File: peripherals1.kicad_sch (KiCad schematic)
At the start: 0 parts

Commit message: feat: add components to peripherals1
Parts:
- added BZ1: Buzzer, https://www.digikey.com.br/en/products/detail/murata-electronics/PKHPS0013E4000-A2/16399967?s=N4IgTCBcDaIAoGkAScDKAGdBG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, symbol Device:Buzzer
- added C1: 1μ, https://www.digikey.com.br/en/products/detail/samsung-electro-mechanics/CL05A105KO5NNNC/3886725?s=N4IgTCBcDaIMIBkAMBWAg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, symbol Device:C
- added D1, D2, D3, D4, D5: LED_GREEN, symbol Device:LED
- added D2: WS2812B, https://www.digikey.com.br/en/products/detail/feztek/FZ2812-5050/18647407?s=N4IgTCBcDaIGIC0wA4CMYC0BWADLkAugL5A, symbol LED:WS2812B
- added D6: LED_RED, symbol Device:LED
- added D7: LED_YELLOW, symbol Device:LED
- added D8: LED_BLUE, symbol Device:LED
- added MK2: Microphone_Condenser, https://www.digikey.com.br/en/products/detail/same-sky-formerly-cui-devices/CMEJ-0415-42-P/10253451?s=N4IgTCBcDaIMIFkCi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, symbol Device:Microphone_Condenser
- added Q1: Q_NMOS_GSD, https://www.digikey.com.br/en/products/detail/diodes-incorporated/DMN2600UFB-7/4249927?s=N4IgTCBcDaICIFkByYBsAGdBVAYgIQ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, symbol Transistor_FET:Q_NMOS_GSD
- added R1: R_Photo, https://www.digikey.com.br/en/products/detail/harvatek-corporation/B13V1IR-20C000114U1930/13574162?s=N4IgTCBcDaIEIEYDMA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, symbol Device:R_Photo
- added R10, R11, R12, R13, R2, R3, R4, R6, R7, R8, R9: 10k, https://www.digikey.com.br/en/products/detail/yageo/RC0402JR-0710KL/726418?s=N4IgTCBcDaIEoGEAMAWJYBScC0SDsAjEgNIAyIAugL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, symbol Device:R
- added R14, R15, R16, R17, R18, R19, R20, R21: 220, symbol Device:R
- added R22: 1k, https://www.digikey.com.br/en/products/detail/yageo/RC0402JR-071KL/726408, symbol Device:R
- added R5: 2.2k, https://www.digikey.com.br/en/products/detail/panasonic-electronic-components/ERA-2AEB222X/1706013, symbol Device:R
- added RV1, RV2: R_Potentiometer, symbol Device:R_Potentiometer
- added SW1, SW2, SW3, SW4, SW5, SW6, SW7, SW8: SW_Push, https://www.digikey.com.br/en/products/detail/c-k/PTS636SM43SMTR-LFS/10071723?s=N4IgTCBcDaIAoBUDKA2AzCpBZALG7CASgAQAyAY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, symbol Switch:SW_Push
- added U1: TSDP343xx, OptoDevice:Vishay_MOLD-3Pin, symbol Interface_Optical:TSDP343xx
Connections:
- new net: D6.2 (A), R19.2
- new net: R3.1, RV1.3
- new net: D8.2 (A), R21.2
- new net: D1.2 (A), R14.2
- new net: D7.2 (A), R20.2
- new net: MK2.1 (-), R5.2
- new net: D4.2 (A), R17.2
- new net: D5.2 (A), R18.2
- new net: D2.2 (A), R15.2
- new net: D3.2 (A), R16.2
- new net: R4.1, RV2.3
- new net +3V3: C1.1, D2.3 (VDD), Q1.3 (D), R1.1, R10.2, R11.2, R12.2, R13.2, R5.1, R6.2, R7.2, R8.2, R9.2, RV1.1, RV2.1
- new net Button1_GPIO: R6.1, SW1.2
- new net Button2_GPIO: R7.1, SW2.2
- new net Button3_GPIO: R8.1, SW3.2
- new net Button4_GPIO: R9.1, SW4.2
- new net Button5_GPIO: R11.1, SW5.2
- new net Button6_GPIO: R12.1, SW6.2
- new net Button7_GPIO: R13.1, SW7.2
- new net Button8_GPIO: R10.1, SW8.2
- new net Buzzer_GPIO: BZ1.1 (+)
- new net GND: BZ1.2 (-), D1.1 (K), D2.1 (K), D2.1 (VSS), D3.1 (K), D4.1 (K), D5.1 (K), D6.1 (K), D7.1 (K), D8.1 (K), MK2.2 (+), Q1.1 (G), Q1.2 (S), R2.2, R22.2, R3.2, R4.2, SW1.1, SW2.1, SW3.1, SW4.1, SW5.1, SW6.1, SW7.1, SW8.1
- new net LDR_ADC: R1.2, R2.1
- new net LED_blue_GPIO: R21.1
- new net LED_end_GPIO: D2.2 (DIN)
- new net LED_green_GPIO: R14.1, R15.1, R16.1, R17.1, R18.1
- new net LED_red_GPIO: R19.1
- new net LED_yellow_GPIO: R20.1
- new net MOSFET_GPIO: R22.1
- new net Microphone_ADC: C1.2
- new net Potentiometer1_ADC: RV1.2
- new net Potentiometer2_ADC: RV2.2
- no-connect marks 0 -> 1

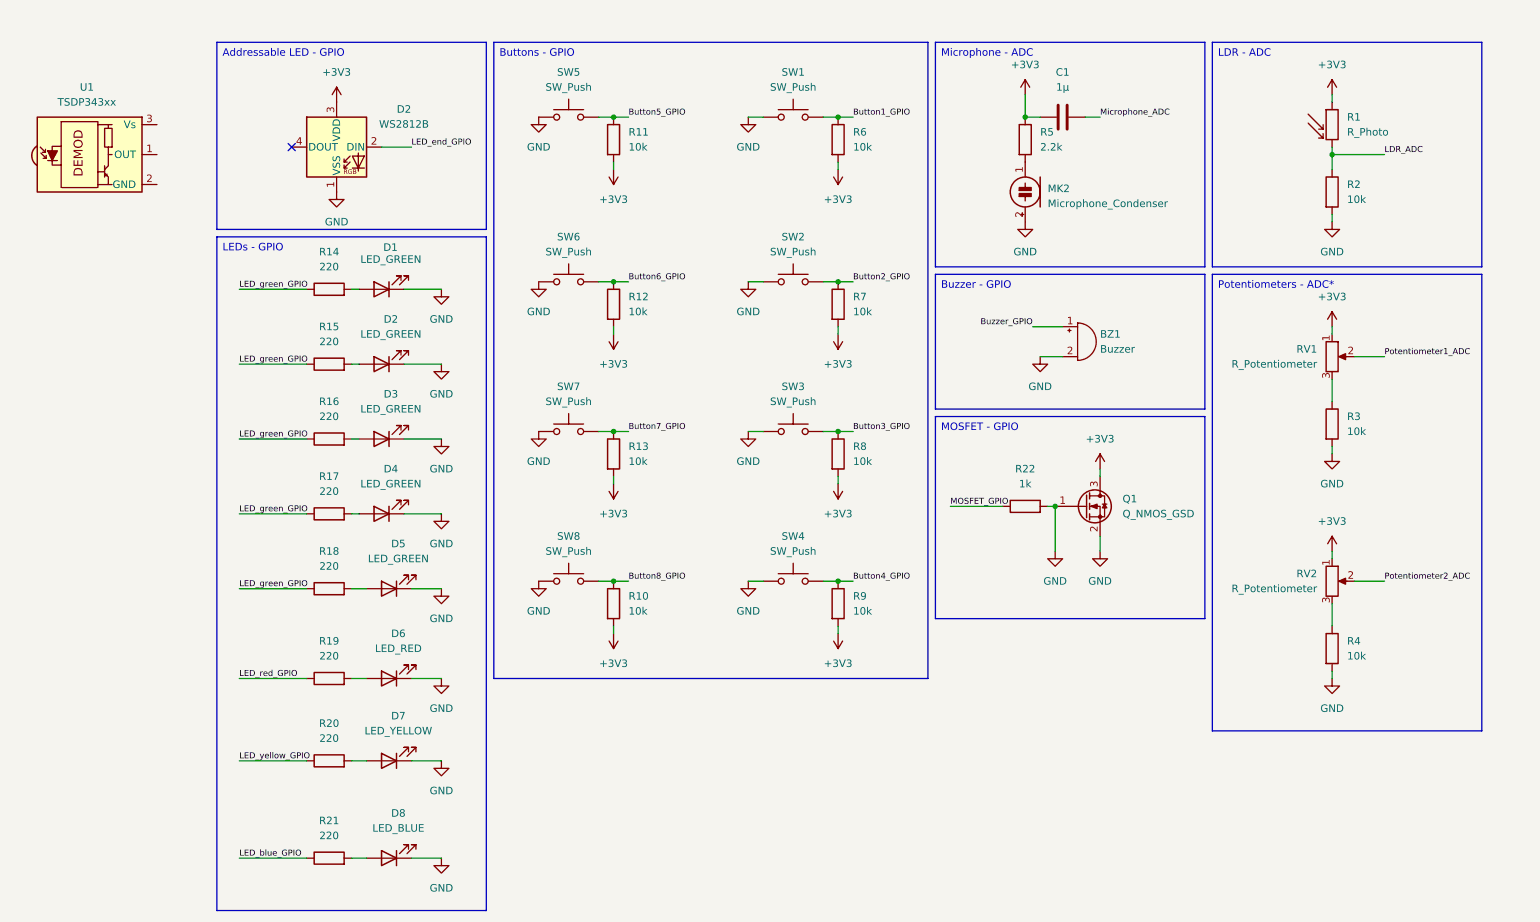
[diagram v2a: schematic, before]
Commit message: refac: changes LED direction, mic output and potentiometer
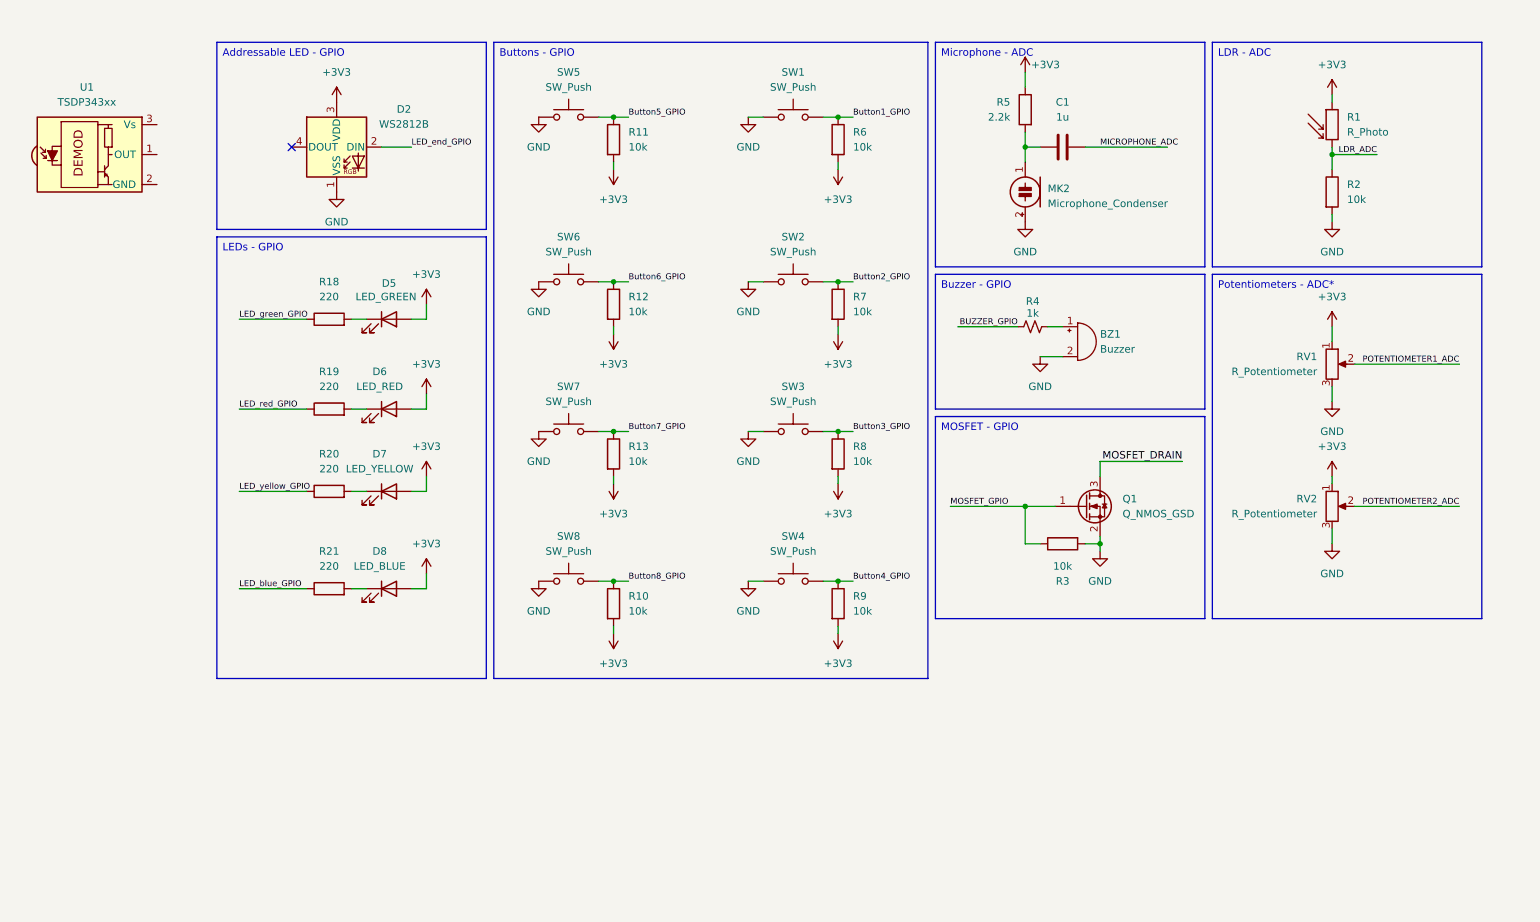
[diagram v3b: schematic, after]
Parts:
- removed D1, D2, D3, D4: LED_GREEN, symbol Device:LED
- removed R14, R15, R16, R17: 220, symbol Device:R
- removed R22: 1k, https://www.digikey.com.br/en/products/detail/yageo/RC0402JR-071KL/726408, symbol Device:R
- removed R4: 10k, https://www.digikey.com.br/en/products/detail/yageo/RC0402JR-0710KL/726418?s=N4IgTCBcDaIEoGEAMAWJYBScC0SDsAjEgNIAyIAugL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, symbol Device:R
- added R4: 1k, Resistor_SMD:R_0402_1005Metric, symbol Device:R_Small_US
- C1: value 1μ -> 1u
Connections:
- net +3V3: now also D5.2 (A), D6.2 (A), D7.2 (A), D8.2 (A); no longer C1.1, Q1.3 (D)
- net GND: now also RV1.3, RV2.3; no longer D5.1 (K), D6.1 (K), D7.1 (K), D8.1 (K), Q1.1 (G)
- net MOSFET_GPIO: now also Q1.1 (G), R3.1
- net at R19.2: now also D6.1 (K); no longer D6.2 (A)
- net at R21.2: now also D8.1 (K); no longer D8.2 (A)
- net at R20.2: now also D7.1 (K); no longer D7.2 (A)
- net at MK2.1 (-), R5.2: now also C1.1
- net at R18.2: now also D5.1 (K); no longer D5.2 (A)
- net Buzzer_GPIO: no longer names the net of BZ1.1 (+)
- net Buzzer_GPIO: now also R4.2
- net Microphone_ADC renamed MICROPHONE_ADC
- net Potentiometer1_ADC renamed POTENTIOMETER1_ADC
- net Potentiometer2_ADC renamed POTENTIOMETER2_ADC
- new net BUZZER_GPIO: R4.1
- new net MOSFET_DRAIN: Q1.3 (D)
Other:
- moved on the sheet: C1, D5, D6, D7, D8, R18, R19, R20, R21, R5, RV1, RV2

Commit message: feat:adds technical informations to components
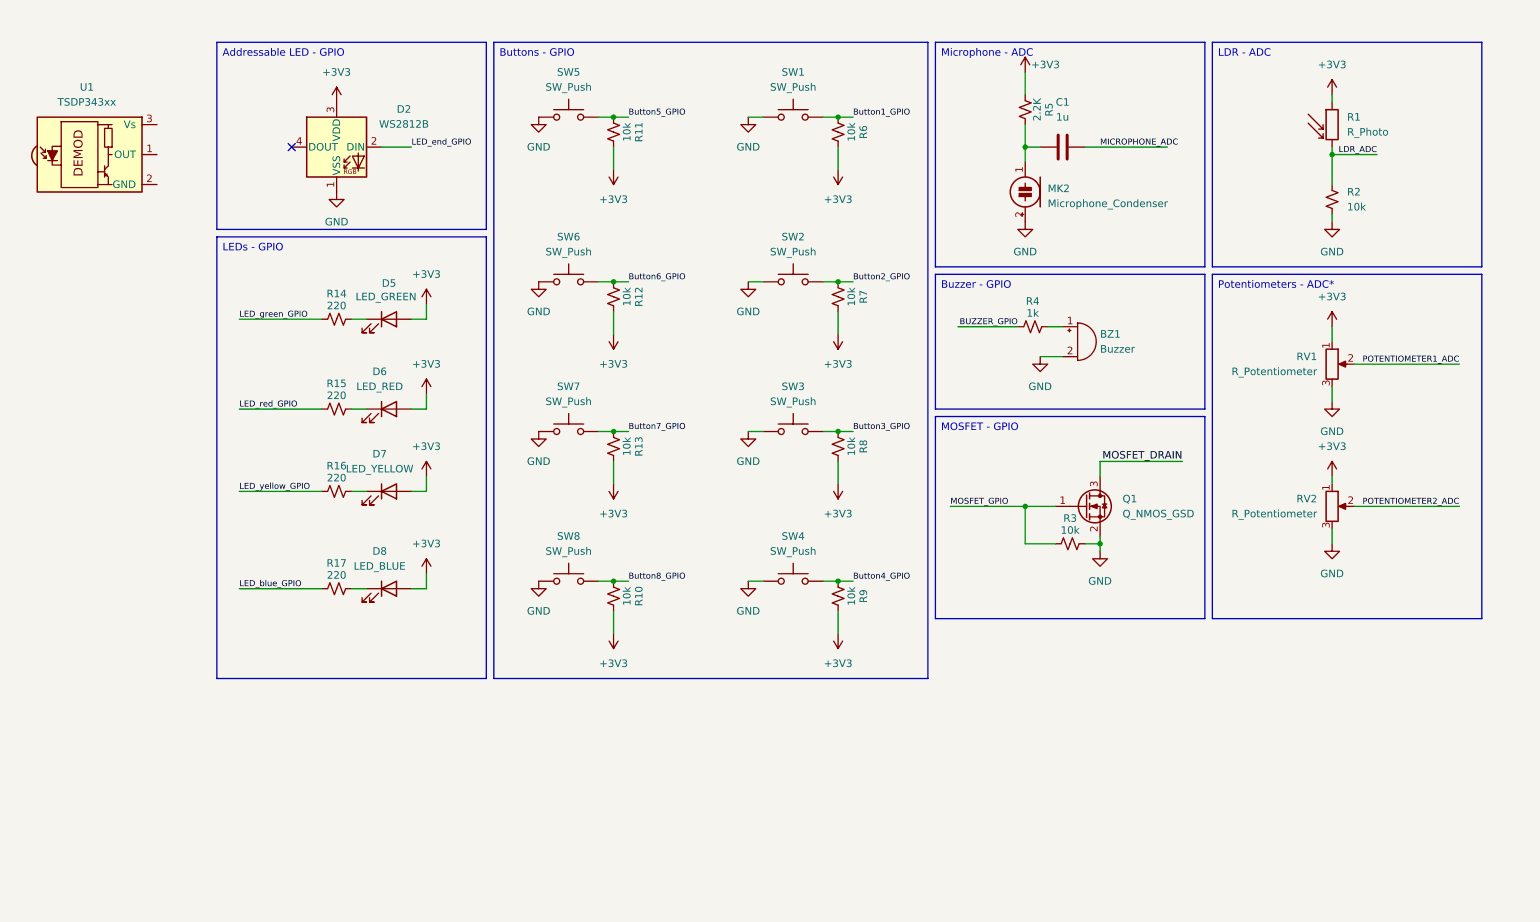
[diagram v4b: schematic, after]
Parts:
- removed R10, R11, R12, R13, R2, R3, R6, R7, R8, R9: 10k, https://www.digikey.com.br/en/products/detail/yageo/RC0402JR-0710KL/726418?s=N4IgTCBcDaIEoGEAMAWJYBScC0SDsAjEgNIAyIAugL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, symbol Device:R
- removed R18, R19, R20, R21: 220, symbol Device:R
- removed R5: 2.2k, https://www.digikey.com.br/en/products/detail/panasonic-electronic-components/ERA-2AEB222X/1706013, symbol Device:R
- added R10, R11, R12, R13, R2, R3, R6, R7, R8, R9: 10k, Resistor_SMD:R_0402_1005Metric, symbol Device:R_Small_US
- added R14, R15, R16, R17: 220, Resistor_SMD:R_0402_1005Metric, symbol Device:R_Small_US
- added R5: 2.2K, Resistor_SMD:R_0402_1005Metric, symbol Device:R_Small_US
- BZ1: footprint https://www.digikey.com.br/en/products/detail/murata-electronics/PKHPS0013E4000-A2/16399967?s=N4IgTCBcDaIAoGkAScDKAGdBG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 -> (none); MPN (none) -> PKHPS0013E4000-A2
- C1: footprint https://www.digikey.com.br/en/products/detail/samsung-electro-mechanics/CL05A105KO5NNNC/3886725?s=N4IgTCBcDaIMIBkAMBWAg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 -> (none); MPN (none) -> CL05A105KO5NNNC
- D2: footprint https://www.digikey.com.br/en/products/detail/feztek/FZ2812-5050/18647407?s=N4IgTCBcDaIGIC0wA4CMYC0BWADLkAugL5A -> (none); MPN (none) -> FZ2812-5050
- D5: MPN (none) -> LGR971-KN-1
- D6: MPN (none) -> QBLP601-R3-2943
- D7: MPN (none) -> LY Q976.01-Q1R2-36-1
- D8: MPN (none) -> LB Q99G.01-P1R1-35-1-5-R18
- MK2: footprint https://www.digikey.com.br/en/products/detail/same-sky-formerly-cui-devices/CMEJ-0415-42-P/10253451?s=N4IgTCBcDaIMIFkCi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 -> (none); MPN (none) -> CMEJ-0415-42-P
- Q1: footprint https://www.digikey.com.br/en/products/detail/diodes-incorporated/DMN2600UFB-7/4249927?s=N4IgTCBcDaICIFkByYBsAGdBVAYgIQ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 -> (none); MPN (none) -> DMN2600UFB-7
- R1: footprint https://www.digikey.com.br/en/products/detail/harvatek-corporation/B13V1IR-20C000114U1930/13574162?s=N4IgTCBcDaIEIEYDMA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 -> (none); MPN (none) -> FZ2812-5050
- SW1, SW2, SW3, SW4, SW5, SW6, SW7, SW8: footprint https://www.digikey.com.br/en/products/detail/c-k/PTS636SM43SMTR-LFS/10071723?s=N4IgTCBcDaIAoBUDKA2AzCpBZALG7CASgAQAyAY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 -> (none); MPN (none) -> PTS636SM43SMTR LFS
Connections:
- net +3V3: now also R10.2, R11.2, R12.2, R13.2, R5.1, R6.2, R7.2, R8.2, R9.2
- net Button1_GPIO: now also R6.1
- net Button2_GPIO: now also R7.1
- net Button3_GPIO: now also R8.1
- net Button4_GPIO: now also R9.1
- net Button5_GPIO: now also R11.1
- net Button6_GPIO: now also R12.1
- net Button7_GPIO: now also R13.1
- net Button8_GPIO: now also R10.1
- net GND: now also R2.2, R3.2
- net LDR_ADC: now also R2.1
- net LED_blue_GPIO: now also R17.1
- net LED_green_GPIO: now also R14.1
- net LED_red_GPIO: now also R15.1
- net LED_yellow_GPIO: now also R16.1
- net MOSFET_GPIO: now also R3.1
- net at D6.1 (K): now also R15.2
- net at D8.1 (K): now also R17.2
- net at D7.1 (K): now also R16.2
- net at C1.1, MK2.1 (-): now also R5.2
- net at D5.1 (K): now also R14.2

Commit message: refac: reannotates designators
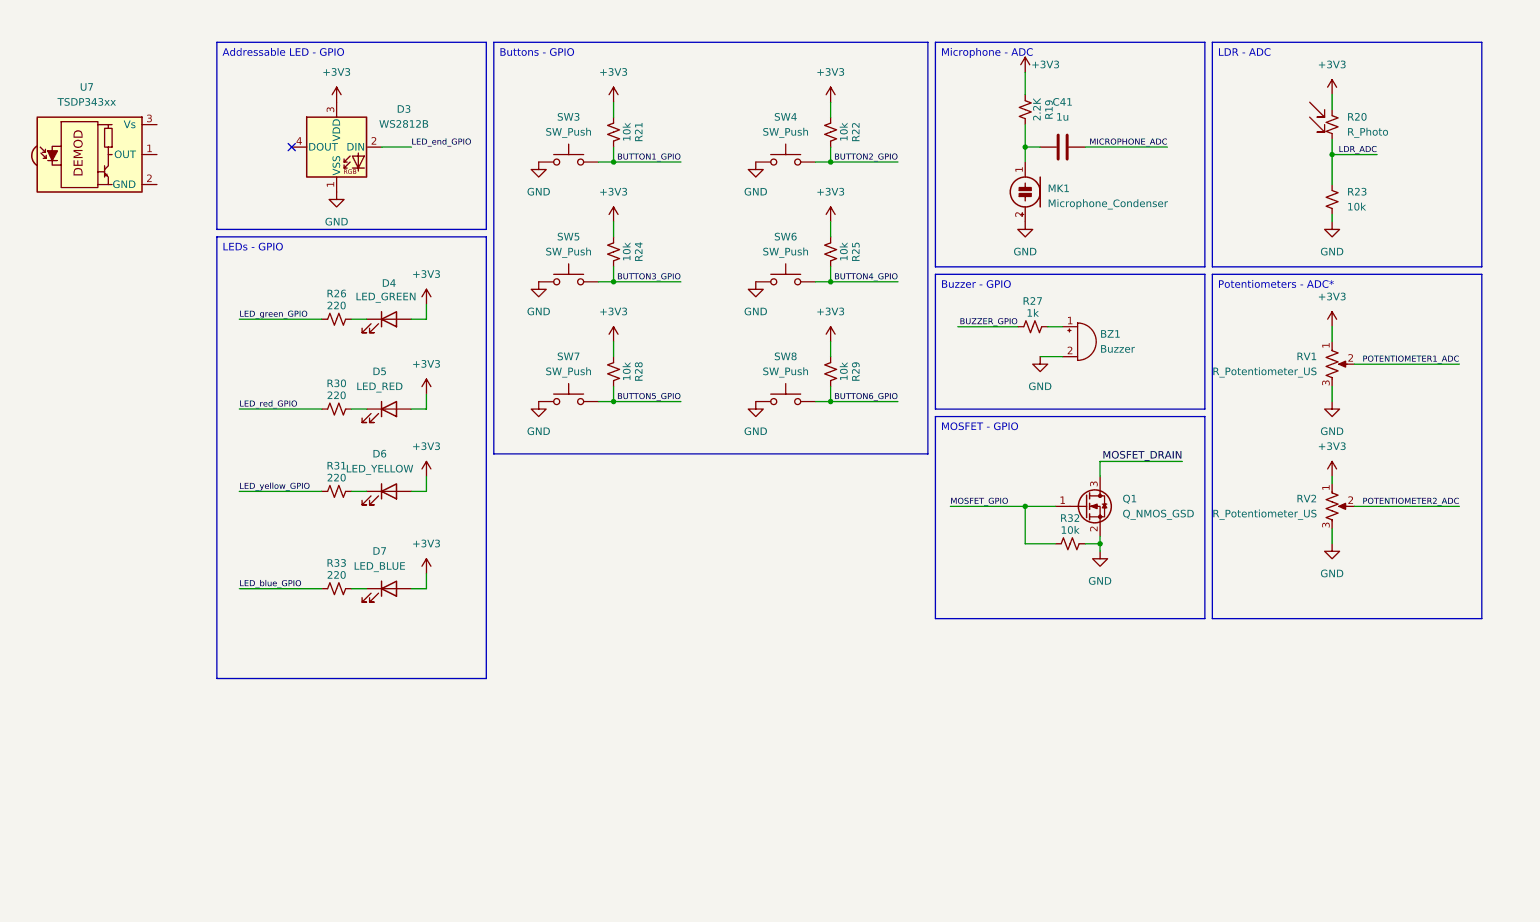
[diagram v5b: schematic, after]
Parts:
- removed R1: R_Photo, symbol Device:R_Photo
- removed R10, R12, R13, R6, R7, R8, R9: 10k, Resistor_SMD:R_0402_1005Metric, symbol Device:R_Small_US
- removed RV1, RV2: R_Potentiometer, symbol Device:R_Potentiometer
- removed SW1, SW2, SW3: SW_Push, symbol Switch:SW_Push
- added R20: R_Photo, symbol Device:R_Small_US
- added R22, R24, R25, R28, R29: 10k, Resistor_SMD:R_0402_1005Metric, symbol Device:R_Small_US
- added RV1, RV2: R_Potentiometer_US, symbol Device:R_Potentiometer_US
- added SW5: SW_Push, symbol Switch:SW_Push
- renumbered C1 to C41, D2 to D3, D5 to D4, D6 to D5, D7 to D6, D8 to D7, MK2 to MK1, R5 to R19, R11 to R21, R2 to R23, R14 to R26, R4 to R27, R15 to R30, R16 to R31, R3 to R32, R17 to R33, SW5 to SW3, U1 to U7
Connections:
- net +3V3: now also R20.1, R22.2, R24.2, R25.2, R28.2, R29.2, RV1.1, RV2.1
- net GND: now also RV1.3, RV2.3, SW5.1
- net LDR_ADC: now also R20.2
- net POTENTIOMETER1_ADC: now also RV1.2
- net POTENTIOMETER2_ADC: now also RV2.2
- net Button4_GPIO renamed BUTTON2_GPIO
- net BUTTON2_GPIO: now also R22.1
- net Button5_GPIO renamed BUTTON1_GPIO
- net Button6_GPIO renamed BUTTON4_GPIO
- net BUTTON4_GPIO: now also R25.1
- net Button7_GPIO renamed BUTTON5_GPIO
- net BUTTON5_GPIO: now also R28.1
- net Button8_GPIO renamed BUTTON6_GPIO
- net BUTTON6_GPIO: now also R29.1
- new net BUTTON3_GPIO: R24.1, SW5.2
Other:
- moved on the sheet: SW3
